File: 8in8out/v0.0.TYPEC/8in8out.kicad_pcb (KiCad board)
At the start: 2 copper layers, 100.1 x 86.4 mm, 61 parts, among them IC1 ATTINY48-A, J1 RJ45, J2 RJ45, J3 CONN_6, K110 G5T-1-12VDC, K120 G5T-1-12VDC, K130 G5T-1-12VDC, K140 G5T-1-12VDC, K150 G5T-1-12VDC, K160 G5T-1-12VDC, K170 G5T-1-12VDC, K180 G5T-1-12VDC, P1 CONN_5, P100 CONN_2, P101 CONN_2, P102 CONN_2, P103 CONN_2, P105 CONN_2, P106 CONN_2, P110 CONN_2, P120 CONN_2, P130 CONN_2, P140 CONN_2, P150 CONN_2, P160 CONN_2, P170 CONN_2, P180 CONN_2, P2 CONN_5, P3 CONN_10X2, P4 CONN_2, U1 7805, U10 OPTO-TRANSISTOR, U2 ULN2803, U20 OPTO-TRANSISTOR, U30 OPTO-TRANSISTOR, U40 OPTO-TRANSISTOR, U50 OPTO-TRANSISTOR, U60 OPTO-TRANSISTOR, U70 OPTO-TRANSISTOR, U80 OPTO-TRANSISTOR

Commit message: correction RJ45 du port I2C
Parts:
- J1, J2: footprint RJ45_8 -> RJ45_BASIC
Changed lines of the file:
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@@
     (links 167)
     (no_connects 0)
-    (area 172.783499 62.534801 290.322002 179.7304)
+    (area 181.419499 70.929499 281.876501 157.670501)
     (thickness 1.6002)
     (drawings 111)
@@
     )
   )
-  (module RJ45_8 (layer Dessus)
-    (at 255.016 149.606)
-    (tags RJ45)
-    (fp_text reference J2 (at 0.254 4.826) (layer F.SilkS)
-      (effects (font (size 1.27 1.27) (thickness 0.3048)))
-    )
-    (fp_text value RJ45 (at 0.14224 -0.1016) (layer F.SilkS)
-      (effects (font (size 1.00076 1.00076) (thickness 0.2032)))
-    )
-    (fp_line (start -7.62 7.874) (end 7.62 7.874) (layer F.SilkS) (width 0.127))
-    (fp_line (start 7.62 7.874) (end 7.62 -10.16) (layer F.SilkS) (width 0.127))
-    (fp_line (start 7.62 -10.16) (end -7.62 -10.16) (layer F.SilkS) (width 0.127))
-    (fp_line (start -7.62 -10.16) (end -7.62 7.874) (layer F.SilkS) (width 0.127))
-    (pad Hole np_thru_hole circle (at 5.93852 0) (size 3.64998 3.64998) (drill 3.251199)
-      (layers *.Cu *.SilkS *.Mask)
-    )
-    (pad Hole np_thru_hole circle (at -5.9309 0) (size 3.64998 3.64998) (drill 3.251199)
-      (layers *.Cu *.SilkS *.Mask)
-    )
-    (pad 1 thru_hole rect (at -4.445 -6.35) (size 1.50114 1.50114) (drill 0.899159)
-      (layers *.Cu *.Mask F.SilkS)
-      (net 94 SDA)
-    )
-    (pad 2 thru_hole circle (at -3.175 -8.89) (size 1.50114 1.50114) (drill 0.899159)
-      (layers *.Cu *.Mask F.SilkS)
-      (net 35 GND)
-    )
-    (pad 3 thru_hole circle (at -1.905 -6.35) (size 1.50114 1.50114) (drill 0.899159)
-      (layers *.Cu *.Mask F.SilkS)
-      (net 93 SCL)
-    )
-    (pad 4 thru_hole circle (at -0.635 -8.89) (size 1.50114 1.50114) (drill 0.899159)
-      (layers *.Cu *.Mask F.SilkS)
-      (net 35 GND)
-    )
-    (pad 5 thru_hole circle (at 0.635 -6.35) (size 1.50114 1.50114) (drill 0.899159)
-      (layers *.Cu *.Mask F.SilkS)
-      (net 19 /INT)
-    )
-    (pad 6 thru_hole circle (at 1.905 -8.89) (size 1.50114 1.50114) (drill 0.899159)
-      (layers *.Cu *.Mask F.SilkS)
-      (net 35 GND)
-    )
-    (pad 7 thru_hole circle (at 3.175 -6.35) (size 1.50114 1.50114) (drill 0.899159)
-      (layers *.Cu *.Mask F.SilkS)
-      (net 20 5V_EXT)
-    )
-    (pad 8 thru_hole circle (at 4.445 -8.89) (size 1.50114 1.50114) (drill 0.899159)
-      (layers *.Cu *.Mask F.SilkS)
-      (net 20 5V_EXT)
-    )
-    (model connectors/RJ45_8.wrl
-      (at (xyz 0 0 0))
-      (scale (xyz 0.4 0.4 0.4))
-      (rotate (xyz 0 0 0))
-    )
-  )
-  (module RJ45_8 (layer Dessus)
-    (at 271.78 149.606)
-    (tags RJ45)
-    (fp_text reference J1 (at 0.254 4.826) (layer F.SilkS)
-      (effects (font (size 1.27 1.27) (thickness 0.3175)))
-    )
-    (fp_text value RJ45 (at 0.14224 -0.1016) (layer F.SilkS)
-      (effects (font (size 1.00076 1.00076) (thickness 0.2032)))
-    )
-    (fp_line (start -7.62 7.874) (end 7.62 7.874) (layer F.SilkS) (width 0.127))
-    (fp_line (start 7.62 7.874) (end 7.62 -10.16) (layer F.SilkS) (width 0.127))
-    (fp_line (start 7.62 -10.16) (end -7.62 -10.16) (layer F.SilkS) (width 0.127))
-    (fp_line (start -7.62 -10.16) (end -7.62 7.874) (layer F.SilkS) (width 0.127))
-    (pad Hole np_thru_hole circle (at 5.93852 0) (size 3.64998 3.64998) (drill 3.251199)
-      (layers *.Cu *.SilkS *.Mask)
-    )
-    (pad Hole np_thru_hole circle (at -5.9309 0) (size 3.64998 3.64998) (drill 3.251199)
-      (layers *.Cu *.SilkS *.Mask)
-    )
-    (pad 1 thru_hole rect (at -4.445 -6.35) (size 1.50114 1.50114) (drill 0.899159)
-      (layers *.Cu *.Mask F.SilkS)
-      (net 94 SDA)
-    )
-    (pad 2 thru_hole circle (at -3.175 -8.89) (size 1.50114 1.50114) (drill 0.899159)
-      (layers *.Cu *.Mask F.SilkS)
-      (net 35 GND)
-    )
-    (pad 3 thru_hole circle (at -1.905 -6.35) (size 1.50114 1.50114) (drill 0.899159)
-      (layers *.Cu *.Mask F.SilkS)
-      (net 93 SCL)
-    )
-    (pad 4 thru_hole circle (at -0.635 -8.89) (size 1.50114 1.50114) (drill 0.899159)
-      (layers *.Cu *.Mask F.SilkS)
-      (net 35 GND)
-    )
-    (pad 5 thru_hole circle (at 0.635 -6.35) (size 1.50114 1.50114) (drill 0.899159)
-      (layers *.Cu *.Mask F.SilkS)
-      (net 19 /INT)
-    )
-    (pad 6 thru_hole circle (at 1.905 -8.89) (size 1.50114 1.50114) (drill 0.899159)
-      (layers *.Cu *.Mask F.SilkS)
-      (net 35 GND)
-    )
-    (pad 7 thru_hole circle (at 3.175 -6.35) (size 1.50114 1.50114) (drill 0.899159)
-      (layers *.Cu *.Mask F.SilkS)
-      (net 20 5V_EXT)
-    )
-    (pad 8 thru_hole circle (at 4.445 -8.89) (size 1.50114 1.50114) (drill 0.899159)
-      (layers *.Cu *.Mask F.SilkS)
-      (net 20 5V_EXT)
-    )
-    (model connectors/RJ45_8.wrl
-      (at (xyz 0 0 0))
-      (scale (xyz 0.4 0.4 0.4))
-      (rotate (xyz 0 0 0))
-    )
-  )
   (module SM1206 (layer Dessus)
     (at 215.9 143.51)
@@
       (rotate (xyz 0 0 0))
     )
+  )
+  (module RJ45_BASIC (layer Dessus)
+    (at 271.78 149.606)
+    (tags RJ45)
+    (fp_text reference J1 (at 0.254 4.826) (layer F.SilkS)
+      (effects (font (thickness 0.3048)))
+    )
+    (fp_text value RJ45 (at 0.14224 -0.1016) (layer F.SilkS)
+      (effects (font (size 1.00076 1.00076) (thickness 0.2032)))
+    )
+    (fp_line (start -7.62 7.874) (end 7.62 7.874) (layer F.SilkS) (width 0.127))
+    (fp_line (start 7.62 7.874) (end 7.62 -10.16) (layer F.SilkS) (width 0.127))
+    (fp_line (start 7.62 -10.16) (end -7.62 -10.16) (layer F.SilkS) (width 0.127))
+    (fp_line (start -7.62 -10.16) (end -7.62 7.874) (layer F.SilkS) (width 0.127))
+    (pad Hole thru_hole circle (at 5.93852 0) (size 3.64998 3.64998) (drill 3.2512)
+      (layers *.Cu *.Mask F.SilkS)
+    )
+    (pad Hole thru_hole circle (at -5.9309 0) (size 3.64998 3.64998) (drill 3.2512)
+      (layers *.Cu *.Mask F.SilkS)
+    )
+    (pad 1 thru_hole rect (at -4.445 -6.35) (size 1.50114 1.50114) (drill 0.89916)
+      (layers *.Cu *.Mask F.SilkS)
+      (net 94 SDA)
+    )
+    (pad 2 thru_hole circle (at -3.175 -8.89) (size 1.50114 1.50114) (drill 0.89916)
+      (layers *.Cu *.Mask F.SilkS)
+      (net 35 GND)
+    )
+    (pad 3 thru_hole circle (at -1.905 -6.35) (size 1.50114 1.50114) (drill 0.89916)
+      (layers *.Cu *.Mask F.SilkS)
+      (net 93 SCL)
+    )
+    (pad 4 thru_hole circle (at -0.635 -8.89) (size 1.50114 1.50114) (drill 0.89916)
+      (layers *.Cu *.Mask F.SilkS)
+      (net 35 GND)
+    )
+    (pad 5 thru_hole circle (at 0.635 -6.35) (size 1.50114 1.50114) (drill 0.89916)
+      (layers *.Cu *.Mask F.SilkS)
+      (net 19 /INT)
+    )
+    (pad 6 thru_hole circle (at 1.905 -8.89) (size 1.50114 1.50114) (drill 0.89916)
+      (layers *.Cu *.Mask F.SilkS)
+      (net 35 GND)
+    )
+    (pad 7 thru_hole circle (at 3.175 -6.35) (size 1.50114 1.50114) (drill 0.89916)
+      (layers *.Cu *.Mask F.SilkS)
+      (net 20 5V_EXT)
+    )
+    (pad 8 thru_hole circle (at 4.445 -8.89) (size 1.50114 1.50114) (drill 0.89916)
+      (layers *.Cu *.Mask F.SilkS)
+      (net 20 5V_EXT)
+    )
+    (model connectors/RJ45_8.wrl
+      (at (xyz 0 0 0))
+      (scale (xyz 0.4 0.4 0.4))
+      (rotate (xyz 0 0 0))
+    )
+  )
+  (module RJ45_BASIC (layer Dessus)
+    (at 255.016 149.606)
+    (tags RJ45)
+    (fp_text reference J2 (at 0.254 4.826) (layer F.SilkS)
+      (effects (font (thickness 0.3048)))
+    )
+    (fp_text value RJ45 (at 0.14224 -0.1016) (layer F.SilkS)
+      (effects (font (size 1.00076 1.00076) (thickness 0.2032)))
+    )
+    (fp_line (start -7.62 7.874) (end 7.62 7.874) (layer F.SilkS) (width 0.127))
+    (fp_line (start 7.62 7.874) (end 7.62 -10.16) (layer F.SilkS) (width 0.127))
+    (fp_line (start 7.62 -10.16) (end -7.62 -10.16) (layer F.SilkS) (width 0.127))
+    (fp_line (start -7.62 -10.16) (end -7.62 7.874) (layer F.SilkS) (width 0.127))
+    (pad Hole thru_hole circle (at 5.93852 0) (size 3.64998 3.64998) (drill 3.2512)
+      (layers *.Cu *.Mask F.SilkS)
+    )
+    (pad Hole thru_hole circle (at -5.9309 0) (size 3.64998 3.64998) (drill 3.2512)
+      (layers *.Cu *.Mask F.SilkS)
+    )
+    (pad 1 thru_hole rect (at -4.445 -6.35) (size 1.50114 1.50114) (drill 0.89916)
+      (layers *.Cu *.Mask F.SilkS)
+      (net 94 SDA)
+    )
+    (pad 2 thru_hole circle (at -3.175 -8.89) (size 1.50114 1.50114) (drill 0.89916)
+      (layers *.Cu *.Mask F.SilkS)
+      (net 35 GND)
+    )
+    (pad 3 thru_hole circle (at -1.905 -6.35) (size 1.50114 1.50114) (drill 0.89916)
+      (layers *.Cu *.Mask F.SilkS)
+      (net 93 SCL)
+    )
+    (pad 4 thru_hole circle (at -0.635 -8.89) (size 1.50114 1.50114) (drill 0.89916)
+      (layers *.Cu *.Mask F.SilkS)
+      (net 35 GND)
+    )
+    (pad 5 thru_hole circle (at 0.635 -6.35) (size 1.50114 1.50114) (drill 0.89916)
+      (layers *.Cu *.Mask F.SilkS)
+      (net 19 /INT)
+    )
+    (pad 6 thru_hole circle (at 1.905 -8.89) (size 1.50114 1.50114) (drill 0.89916)
+      (layers *.Cu *.Mask F.SilkS)
+      (net 35 GND)
+    )
+    (pad 7 thru_hole circle (at 3.175 -6.35) (size 1.50114 1.50114) (drill 0.89916)
+      (layers *.Cu *.Mask F.SilkS)
+      (net 20 5V_EXT)
+    )
+    (pad 8 thru_hole circle (at 4.445 -8.89) (size 1.50114 1.50114) (drill 0.89916)
+      (layers *.Cu *.Mask F.SilkS)
+      (net 20 5V_EXT)
+    )
+    (model connectors/RJ45_8.wrl
+      (at (xyz 0 0 0))
+      (scale (xyz 0.4 0.4 0.4))
+      (rotate (xyz 0 0 0))
+    )

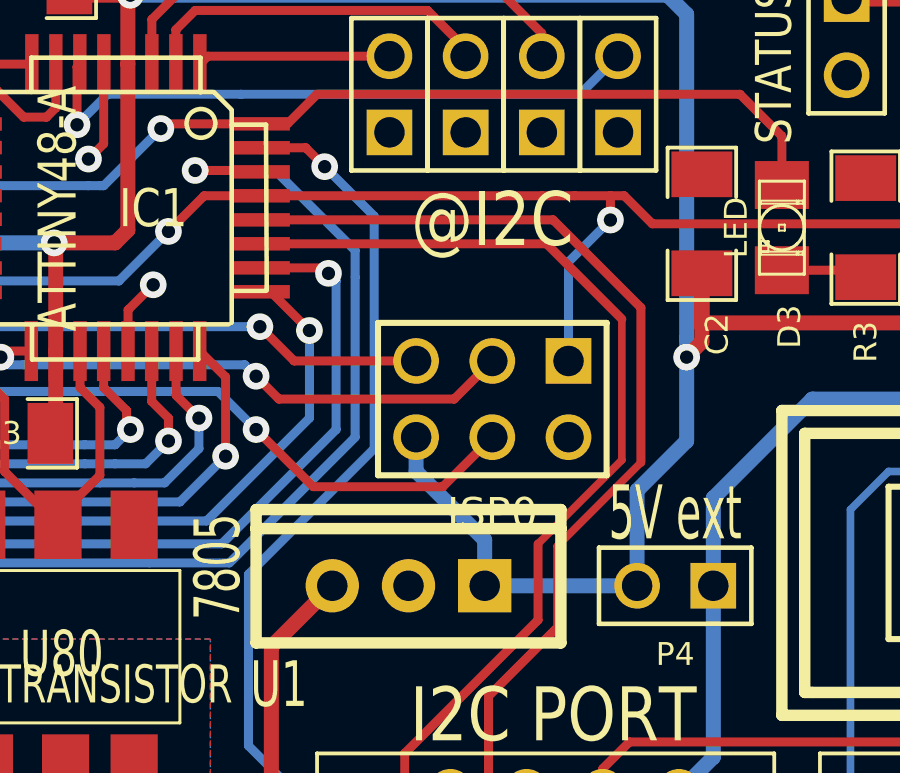
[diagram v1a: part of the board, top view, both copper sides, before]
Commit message: correction connecteur ISP
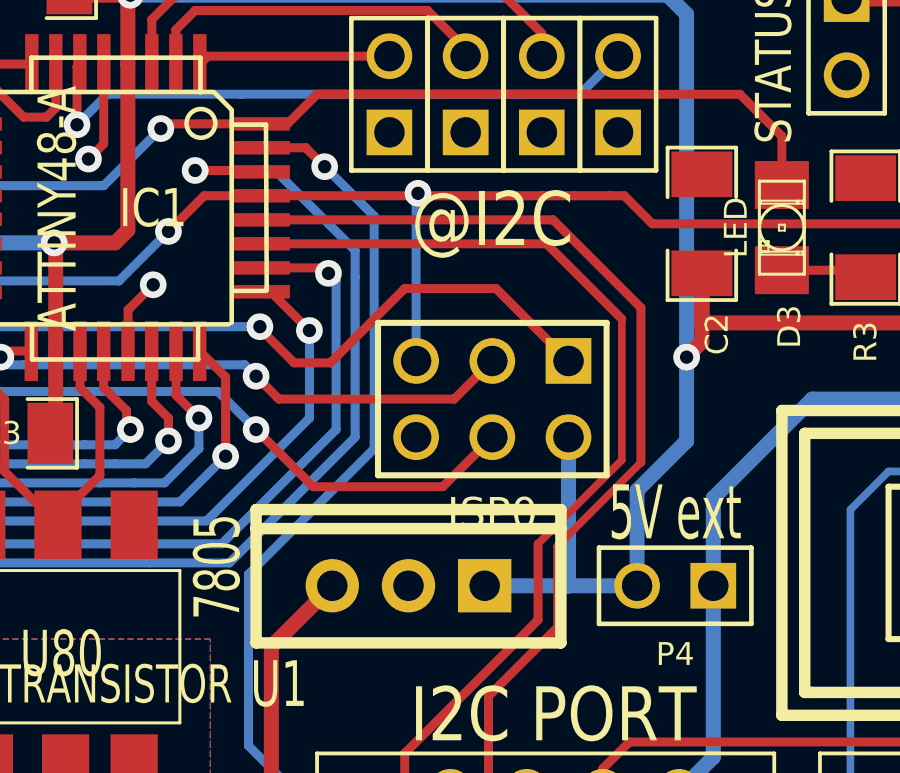
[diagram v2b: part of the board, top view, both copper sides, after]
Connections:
- ISP0 pad 1: RESET -> MISO
- ISP0 pad 2: GND -> +5V
- ISP0 pad 5: MISO -> RESET
- ISP0 pad 6: +5V -> GND
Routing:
- net MISO: track 16.3 -> 23.5 mm
- net +5V: track 115.9 -> 115.2 mm
